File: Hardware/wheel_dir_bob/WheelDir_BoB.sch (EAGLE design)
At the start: 15 parts, among them U1 DUAL-OPTOISOLATOR_SOIC8

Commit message: Deletes uneccessary optoisolator
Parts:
- removed U1: DUAL-OPTOISOLATOR_SOIC8, SparkFun-DiscreteSemi:DUAL-OPTOISOLATOR_SOIC8
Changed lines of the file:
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@@
 <part name="C5" library="SparkFun-Capacitors" deviceset="100PF" device="-0603-50V-5%" value="100pF"/>
 <part name="C6" library="SparkFun-Capacitors" deviceset="1.0NF/1000PF" device="-0603-50V-10%" value="1nF"/>
-<part name="U1" library="SparkFun-DiscreteSemi" deviceset="DUAL-OPTOISOLATOR" device="_SOIC8"/>
 <part name="D1" library="SparkFun-DiscreteSemi" deviceset="DIODE-SCHOTTKY" device="-PMEG4005EJ" value="0.5A/40V/420mV"/>
 </parts>
@@
 <attribute name="VALUE" x="128.524" y="91.821" size="1.778" layer="96" font="vector"/>
 </instance>
-<instance part="U1" gate="G$1" x="129.54" y="132.08" smashed="yes">
-<attribute name="NAME" x="124.46" y="139.954" size="1.778" layer="95" font="vector"/>
-<attribute name="VALUE" x="124.46" y="126.746" size="1.778" layer="96" font="vector" align="top-left"/>
-</instance>
 <instance part="D1" gate="G$1" x="162.56" y="121.92" smashed="yes">

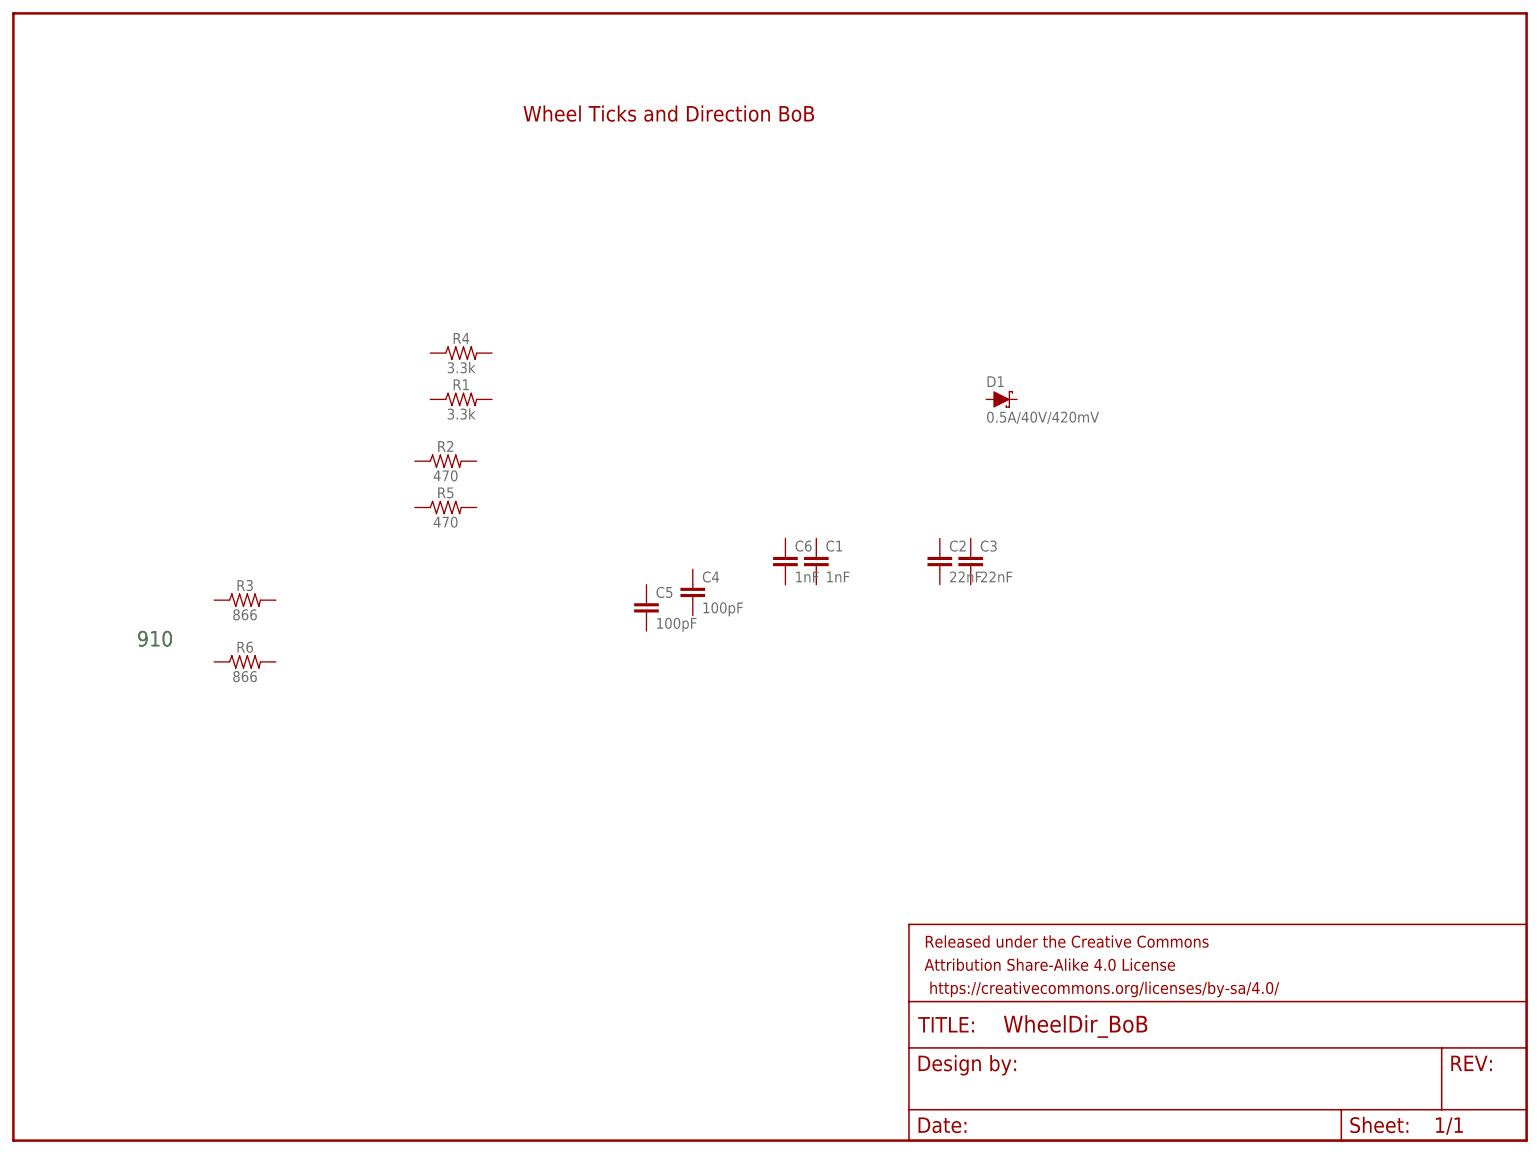
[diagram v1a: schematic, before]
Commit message: Adds the automotive interface breakout board
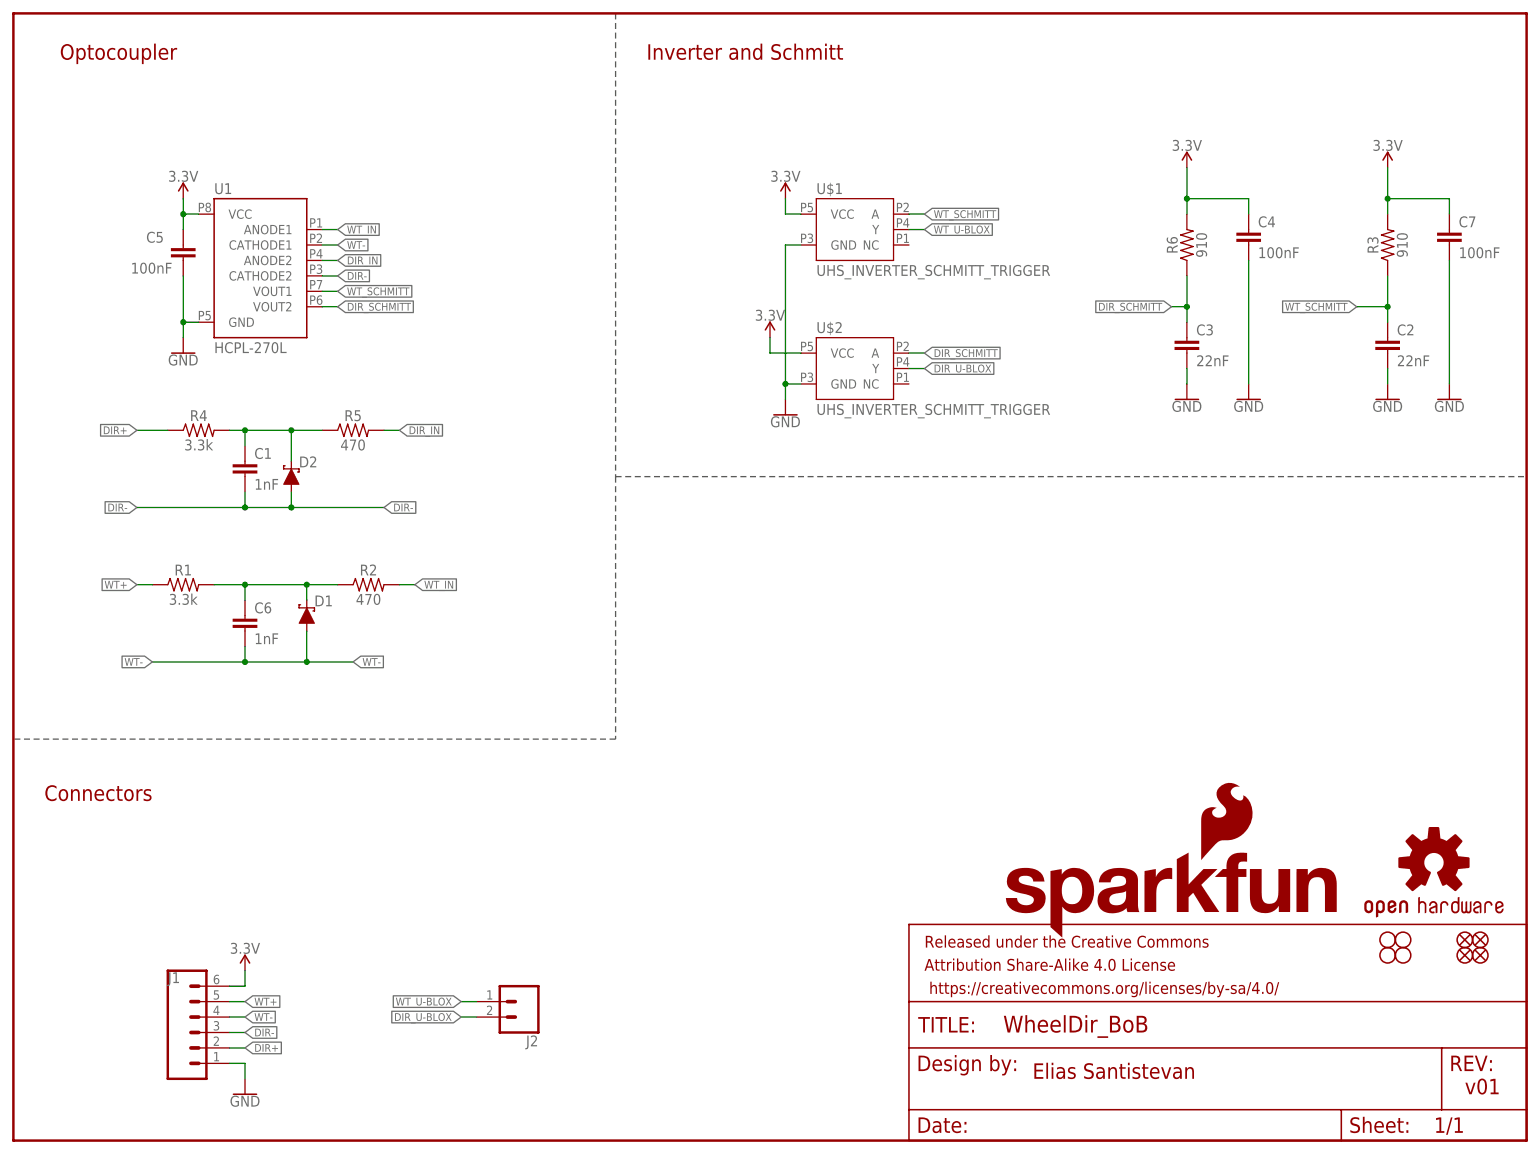
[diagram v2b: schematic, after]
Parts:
- added C7: 100nF, classified:100NF-0603-10V-10%
- added D2: 0.5A/40V/420mV, SparkFun-DiscreteSemi:DIODE-SCHOTTKY-PMEG4005EJ
- added FD1, FD2, FD3, FD4: FIDUCIALUFIDUCIAL, SparkFun-Aesthetics:FIDUCIALUFIDUCIAL
- added H1, H2, H3, H4: STAND-OFF, SparkFun-Hardware:STAND-OFF
- added J1: (no value), SparkFun-Connectors:CONN_06NO_SILK_NO_POP
- added J2: (no value), SparkFun-Connectors:CONN_021X02_NO_SILK
- added LOGO1: SFE_LOGO_NAME_FLAME.1_INCH, SparkFun-Aesthetics:SFE_LOGO_NAME_FLAME.1_INCH
- added LOGO2: OSHW-LOGOS, SparkFun-Aesthetics:OSHW-LOGOS
- added U$1, U$2: UHS_INVERTER_SCHMITT_TRIGGER, classified:UHS_INVERTER_SCHMITT_TRIGGER
- added U1: HCPL-270L, classified:HCPL-270L
- C4, C5: value 100pF -> 100nF; device SparkFun-Capacitors:100PF-0603-50V-5% -> classified:100NF-0603-10V-10%
- R3, R6: value 866 -> 910; device SparkFun-Resistors:866OHM-0603-1/10W-1% -> classified:910OHM-0603-1/10W-5%
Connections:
- new net 3.3V: C4.1, C5.1, C7.1, J1.6, R3.2, R6.2, U$1.VCC, U$2.VCC, U1.VCC
- new net DIR+: J1.2, R4.1
- new net DIR-: C1.2, D2.A, J1.3, U1.CATHODE2
- new net DIR_IN: R5.2, U1.ANODE2
- new net DIR_SCHMITT: C3.1, R6.1, U$2.A, U1.VOUT2
- new net DIR_U-BLOX: J2.2, U$2.Y
- new net GND: C2.2, C3.2, C4.2, C5.2, C7.2, J1.1, U$1.GND, U$2.GND, U1.GND
- new net N$2: C6.1, D1.C, R1.2, R2.1
- new net N$3: C1.1, D2.C, R4.2, R5.1
- new net WT+: J1.5, R1.1
- new net WT-: C6.2, D1.A, J1.4, U1.CATHODE1
- new net WT_IN: R2.2, U1.ANODE1
- new net WT_SCHMITT: C2.1, R3.1, U$1.A, U1.VOUT1
- new net WT_U-BLOX: J2.1, U$1.Y
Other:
- note added: "Connectors"
- note added: "Elias Santistevan"
- note added: "Inverter and Schmitt"
- note added: "Optocoupler"
- note added: "v01"
- note removed: "910"
- note removed: "Wheel Ticks and Direction BoB"
- moved on the sheet: C1, C2, C3, C4, C5, C6, D1, R1, R2, R3, R4, R5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
